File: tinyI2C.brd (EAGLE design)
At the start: 100 x 80 mm, 0 parts

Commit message: sch and brd update
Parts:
- added C1, C2, C3, C4, C6: 1005, rcl:C1005
- added C5: 1608, rcl:C1608
- added IC1: 74ABT125BQ, 74xx-eu_local:DHVQFN14
- added IC2: TPS76318, texas:SOT23-DBV
- added R1, R2: 220/1005, rcl:R1005
- added R10, R3, R4, R5, R6, R7, R8, R9: 10k/1005, rcl:R1005
- added TP1, TP2, TP3, TP8, TP9: TPTP07R, testpad:TP07R
- added U1: LPC824M201JHI33, mbed-HDK:HVQFN33
- added X1, X3: TSW-112-02-S-S, con-samtec.local:TSW-112-02-S-S
- added X2: TSW-106-02-S-S-RA, con-samtec.local:TSW-106-02-S-S-RA
- added X4: TSW-102-02-S-S, con-samtec.local:TSW-102-02-S-S
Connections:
- new net !ISP!: R3.1, U1.2, X1.3
- new net !RESET!: R4.1, U1.3, X4.1
- new net 1.8V: C1.1, C2.1, C4.1, C6.1, IC1.14, IC2.5, R1.2, R10.2, R2.2, R3.2, R4.2, R5.2, R6.2, R7.2, R8.2, R9.2, TP2.TP, U1.19, U1.21, X1.1
- new net 5V: C5.1, IC2.1, IC2.3, TP1.TP, X2.3
- new net CTS<-: IC1.6, X2.2
- new net GND: C1.2, C2.2, C3.2, C4.2, C5.2, C6.2, IC1.1, IC1.10, IC1.13, IC1.4, IC1.7, IC1.EXP, IC2.2, TP3.TP, U1.20, U1.EXP, X1.2, X2.1, X4.2
- new net GPIO00: U1.32, X3.1
- new net GPIO01: U1.31, X3.2
- new net GPIO02: U1.30, X3.3
- new net GPIO03: U1.29, X3.4
- new net GPIO04: U1.28, X3.5
- new net GPIO05: U1.27, X3.6
- new net GPIO06: U1.26, X3.7
- new net GPIO07: U1.25, X3.8
- new net GPIO10: R10.1, U1.15, X1.12
- new net GPIO11: R9.1, U1.14, X1.11
- new net GPIO12: R8.1, U1.13, X1.10
- new net GPIO13: R7.1, U1.12, X1.9
- new net GPIO14: R6.1, U1.11, X1.8
- new net GPIO15: R5.1, U1.10, X1.7
- new net GPIO16: U1.5, X1.4
- new net I2C_SCL: R2.1, U1.9, X1.6
- new net I2C_SDA: R1.1, U1.8, X1.5
- new net N$1: C3.1, IC2.4
- new net RTS->: IC1.9, X2.6
- new net RX<-: IC1.11, X2.5
- new net SPI_CS: U1.17, X3.12
- new net SPI_MISO: U1.22, X3.10
- new net SPI_MOSI: U1.23, X3.9
- new net SPI_SCK: U1.18, X3.11
- new net SWCLK: TP8.TP, U1.6
- new net SWDIO: TP9.TP, U1.7
- new net TGT_CTS: IC1.8, U1.16
- new net TGT_RTS: IC1.5, U1.1
- new net TGT_RX: IC1.3, U1.24
- new net TGT_TX: IC1.12, U1.4
- new net TX->: IC1.2, X2.4
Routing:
- net 1.8V: track 0.00 -> 49.3 mm, vias 0 -> 15
- net TGT_CTS: track 0.00 -> 24.3 mm, vias 0 -> 2
- net SPI_CS: track 0.00 -> 19.7 mm
- net GPIO00: track 0.00 -> 18.6 mm, vias 0 -> 1
- net SPI_SCK: track 0.00 -> 17.9 mm
- net !RESET!: track 0.00 -> 17.8 mm, vias 0 -> 2
- net TGT_RX: track 0.00 -> 17.3 mm, vias 0 -> 2
- net GPIO01: track 0.00 -> 16.7 mm, vias 0 -> 1
- net !ISP!: track 0.00 -> 15.6 mm, vias 0 -> 2
- net GND: track 0.00 -> 15.6 mm, vias 0 -> 13
- net TGT_TX: track 0.00 -> 15.5 mm, vias 0 -> 2
- net CTS<-: track 0.00 -> 15.1 mm
- net GPIO02: track 0.00 -> 15.0 mm
- net GPIO10: track 0.00 -> 14.6 mm
- net GPIO11: track 0.00 -> 14.1 mm
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- added copper zone on layer 16, net 1.8V
- added copper zone on layer 1, net GND
- added copper zone on layer 16, net GND
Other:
- board size 100 x 80 mm -> 80.8 x 80 mm

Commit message: fiducials
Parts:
- added TP4, TP5: TPTP10R, testpad:TP10R
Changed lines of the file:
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@@
 <hole x="5" y="75" drill="4"/>
 <hole x="75.8" y="5" drill="4"/>
-<polygon width="0.2" layer="29">
+<polygon width="0" layer="29">
 <vertex x="69.8" y="4"/>
 <vertex x="69.8" y="6"/>
@@
 <vertex x="71.8" y="4"/>
 </polygon>
-<polygon width="0.2" layer="29">
+<polygon width="0" layer="29">
 <vertex x="14" y="74"/>
 <vertex x="14" y="76"/>
@@
 <attribute name="VALUE" x="17.72" y="20.355" size="1.27" layer="27" rot="R180"/>
 </element>
+<element name="TP4" library="testpad" package="TP10R" value="TPTP10R" x="15" y="75" smashed="yes">
+<attribute name="TP_SIGNAL_NAME" value="" x="15" y="73.095" size="1" layer="37"/>
+<attribute name="VALUE" x="14.746" y="74.492" size="0.0254" layer="27"/>
+</element>
+<element name="TP5" library="testpad" package="TP10R" value="TPTP10R" x="70.8" y="5" smashed="yes">
+<attribute name="TP_SIGNAL_NAME" value="" x="70.8" y="3.095" size="1" layer="37"/>
+<attribute name="VALUE" x="70.546" y="4.492" size="0.0254" layer="27"/>
+</element>
 </elements>

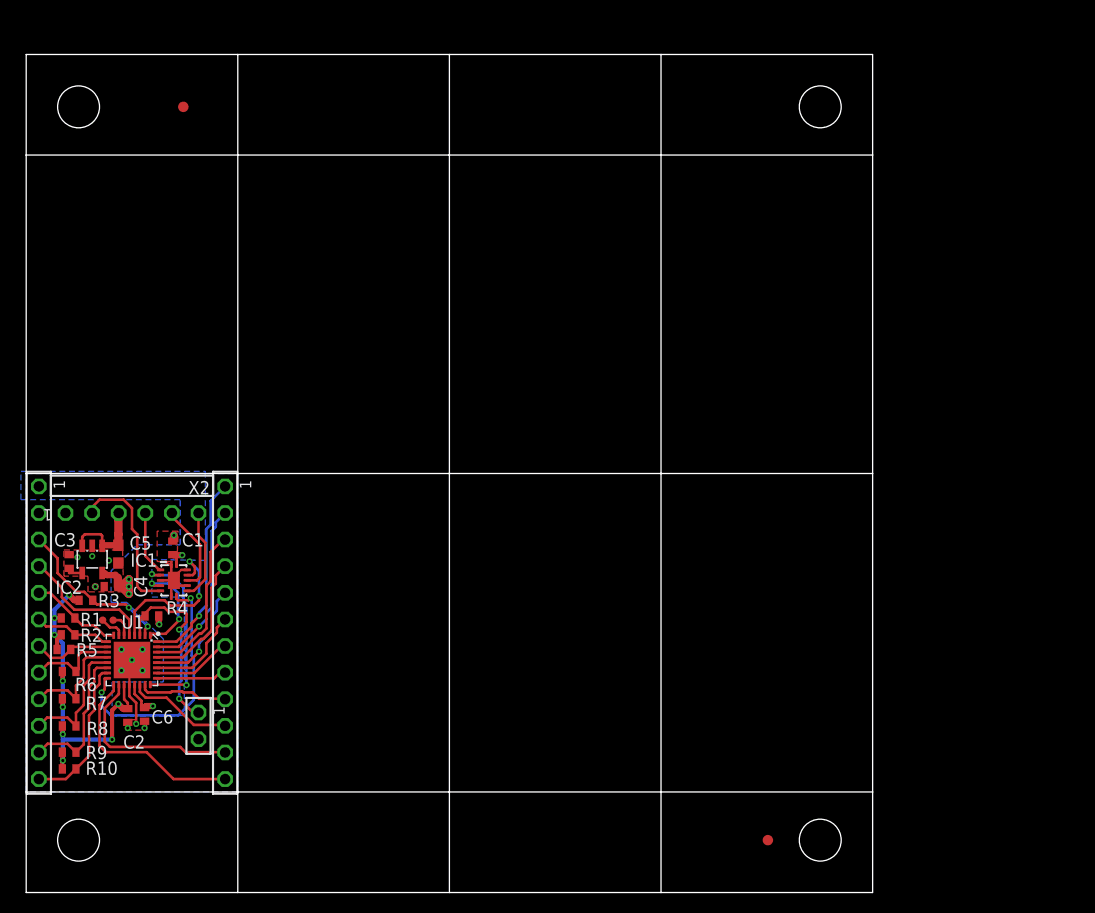
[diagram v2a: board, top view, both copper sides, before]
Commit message: panelize update
each edge has 0.4mm margin
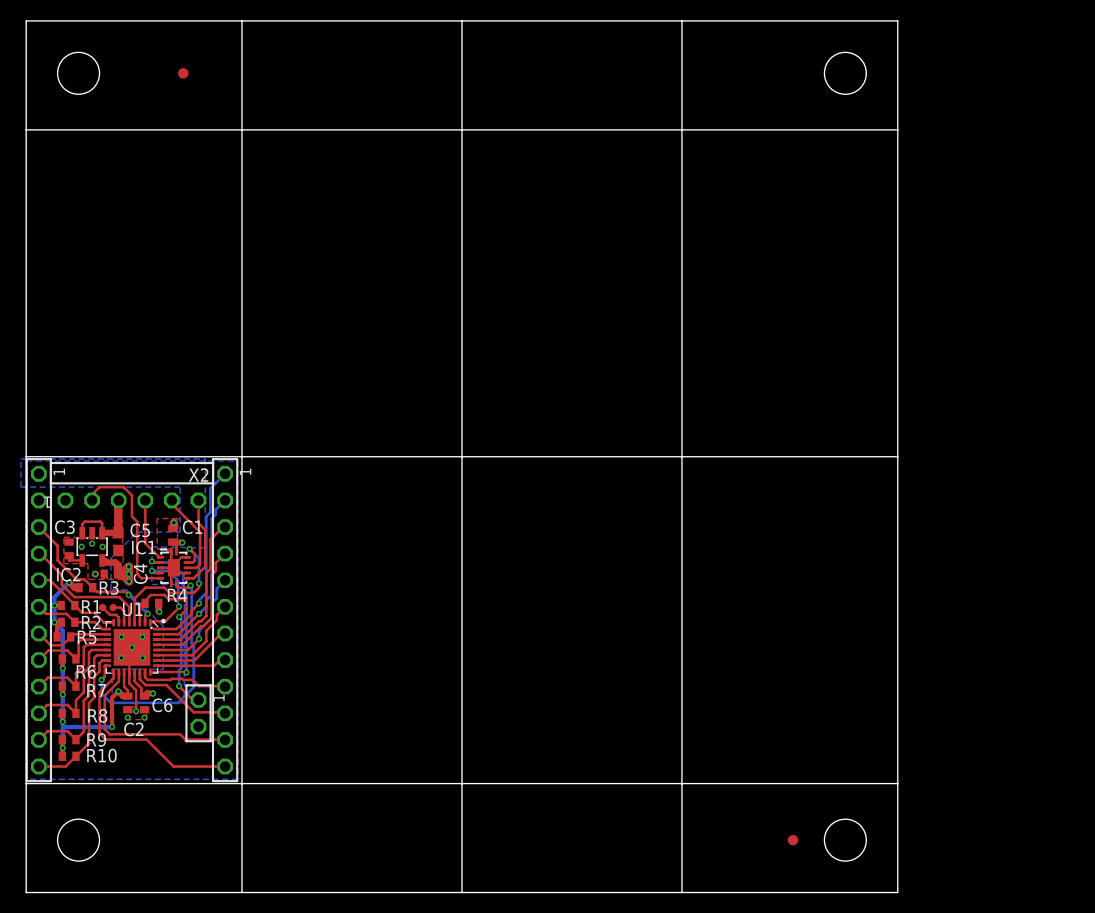
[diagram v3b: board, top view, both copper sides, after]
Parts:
- moved TP4 3.20 mm to (15.0, 78.2)
- moved TP5 2.40 mm to (73.2, 5.00)
- moved C1 1.20 mm to (14.0, 34.1)
- moved C2 1.20 mm to (9.70, 18.1)
- moved C5 1.20 mm to (8.80, 33.5)
- moved R3 1.20 mm to (5.70, 29.1)
- moved R4 1.20 mm to (12.0, 27.6)
- moved X2 1.20 mm to (10.1, 39.0)
- moved R8 1.20 mm to (4.10, 17.1)
- moved C4 1.20 mm to (8.10, 30.4)
- moved IC1 1.20 mm to (14.1, 31.0)
- moved IC2 1.20 mm to (6.30, 33.0)
- moved R1 1.20 mm to (4.00, 27.4)
- moved R10 1.20 mm to (4.10, 13.0)
- moved R2 1.20 mm to (4.00, 25.8)
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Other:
- board size 80.8 x 80 mm -> 83.2 x 83.2 mm

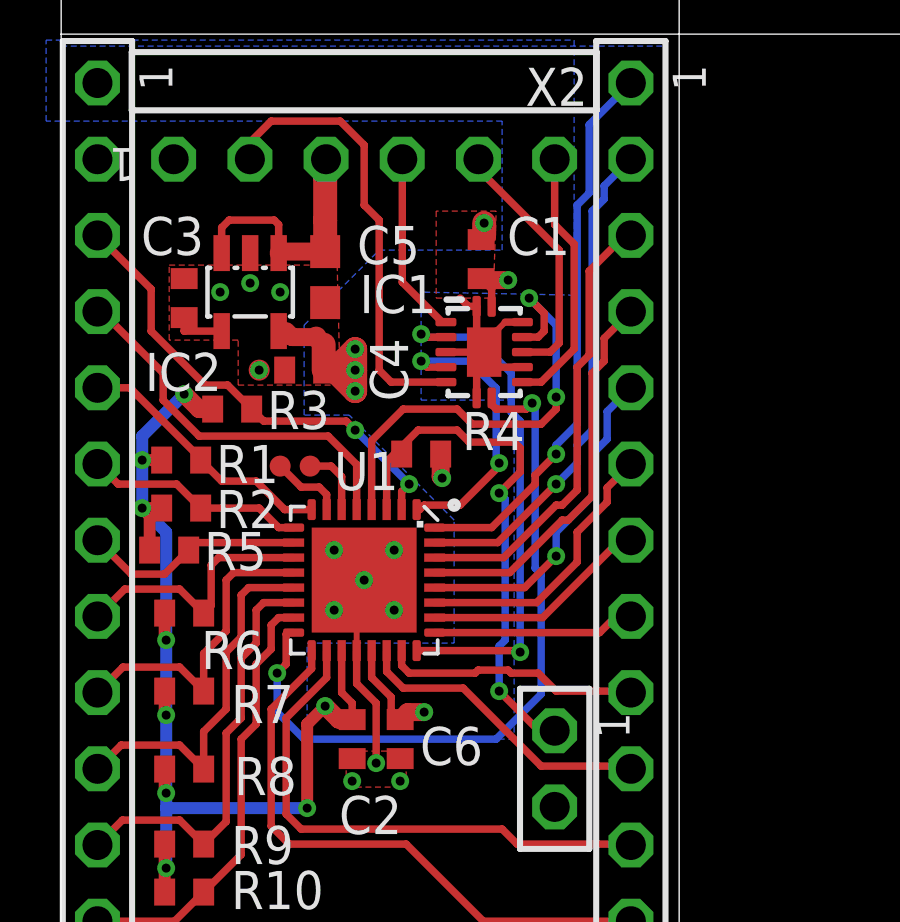
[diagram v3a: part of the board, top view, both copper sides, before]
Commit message: 1.8V trace get wider
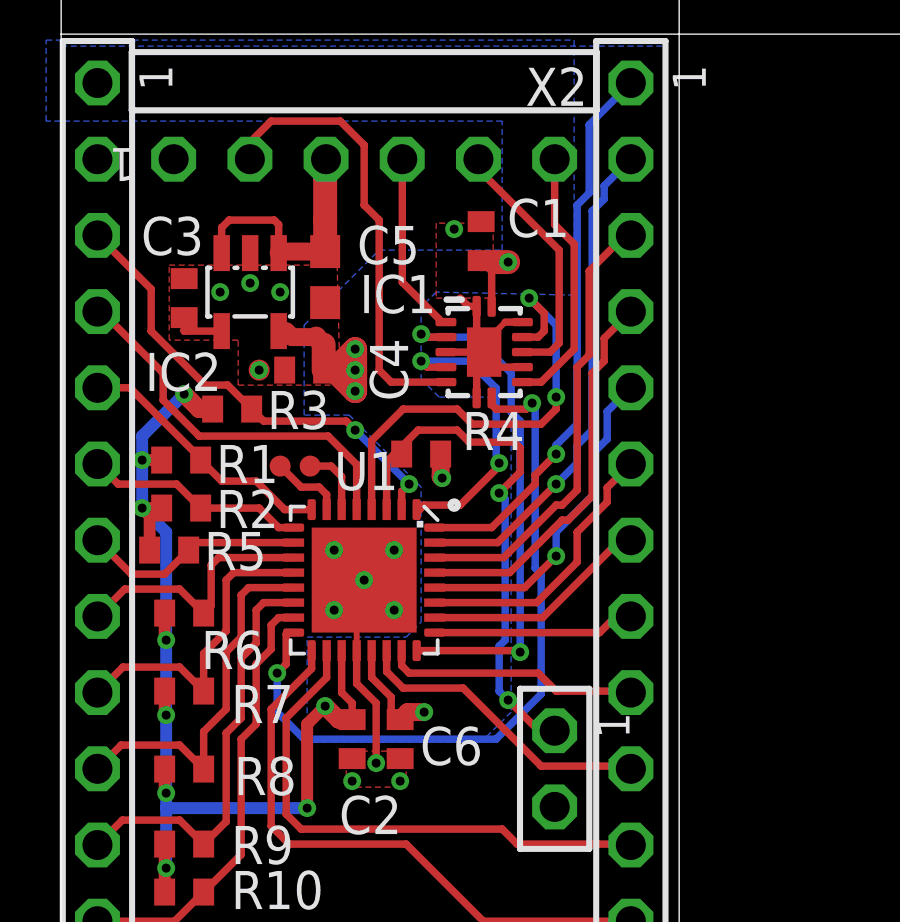
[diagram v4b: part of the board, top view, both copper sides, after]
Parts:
- moved C1 0.60 mm to (14.0, 34.7)
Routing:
- net 1.8V: track 49.4 -> 50.1 mm
- net GND: track 15.6 -> 15.0 mm
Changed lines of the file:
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@@
 <attribute name="VALUE" x="8.205" y="36.429" size="1.27" layer="27" rot="R180"/>
 </element>
-<element name="C1" library="rcl" package="C1005" value="1005" x="14" y="34.1" smashed="yes" rot="R90">
-<attribute name="NAME" x="14.865" y="34.235" size="1.27" layer="25" font="vector" ratio="10"/>
-<attribute name="VALUE" x="15.905" y="33.465" size="1.27" layer="27" rot="R90"/>
+<element name="C1" library="rcl" package="C1005" value="1005" x="14" y="34.7" smashed="yes" rot="R90">
+<attribute name="NAME" x="14.865" y="34.835" size="1.27" layer="25" font="vector" ratio="10"/>
+<attribute name="VALUE" x="15.905" y="34.065" size="1.27" layer="27" rot="R90"/>
 </element>
 <element name="C2" library="rcl" package="C1005" value="1005" x="9.7" y="18.1" smashed="yes" rot="R270">
@@
 <contactref element="C2" pad="2"/>
 <contactref element="TP3" pad="TP"/>
-<via x="14.1" y="35.3" extent="1-16" drill="0.3"/>
+<via x="13.1" y="35.1" extent="1-16" drill="0.3"/>
 <via x="11.1" y="22.4" extent="1-16" drill="0.3"/>
 <via x="11.1" y="24.4" extent="1-16" drill="0.3"/>
@@
 <contactref element="C3" pad="2"/>
 <via x="5.3" y="33" extent="1-16" drill="0.3"/>
-<wire x1="14" y1="34.75" x2="14.1" y2="34.9" width="0.6" layer="1"/>
-<wire x1="14.1" y1="34.9" x2="14.1" y2="35.3" width="0.8" layer="1"/>
 <contactref element="X1" pad="2"/>
 <contactref element="C6" pad="2"/>
@@
 <vertex x="12.5" y="32.8"/>
 <vertex x="14.4" y="32.8"/>
-<vertex x="14.5" y="35.7"/>
-<vertex x="12.5" y="35.7"/>
+<vertex x="14.4" y="35.3"/>
+<vertex x="12.5" y="35.3"/>
 </polygon>
 <contactref element="IC1" pad="7"/>
@@
 <contactref element="C2" pad="1"/>
 <contactref element="TP2" pad="TP"/>
-<via x="14.9" y="33.4" extent="1-16" drill="0.3"/>
+<via x="14.9" y="34" extent="1-16" drill="0.3"/>
 <contactref element="R1" pad="2"/>
 <contactref element="R2" pad="2"/>
@@
 <vertex x="17.1" y="41.4"/>
 <vertex x="17.1" y="32.9"/>
-<vertex x="12" y="33"/>
-<vertex x="12" y="29.4"/>
-<vertex x="15.1" y="29.4"/>
-<vertex x="15.1" y="18.1"/>
-<vertex x="8.2" y="18.1"/>
-<vertex x="8.2" y="21.3"/>
-<vertex x="13.1" y="21.3"/>
-<vertex x="13.1" y="25.4"/>
+<vertex x="12.5" y="33"/>
+<vertex x="12" y="32.5"/>
+<vertex x="12" y="30.1"/>
+<vertex x="12.6" y="29.5"/>
+<vertex x="15" y="29.5"/>
+<vertex x="15" y="19"/>
+<vertex x="14" y="18"/>
+<vertex x="8.2" y="18"/>
+<vertex x="8.2" y="21.5"/>
+<vertex x="11.5" y="21.5"/>
+<vertex x="12" y="22"/>
+<vertex x="12" y="26.5"/>
 <vertex x="9.6" y="28.9"/>
 <vertex x="8.1" y="28.9"/>
@@
 <wire x1="7.5" y1="31.7" x2="7.7" y2="31.5" width="0.6" layer="1"/>
 <wire x1="7.7" y1="31.5" x2="8.5" y2="31.5" width="0.6" layer="1"/>
-<wire x1="14.35" y1="33.1" x2="14" y2="33.45" width="0.25" layer="1"/>
 <wire x1="12.65" y1="27.6" x2="12.65" y2="26.85" width="0.6" layer="1"/>
 <wire x1="12.65" y1="26.85" x2="12.7" y2="26.8" width="0.6" layer="1"/>
@@
 <wire x1="2.7" y1="28.2" x2="4.1" y2="29.6" width="0.4" layer="16"/>
 <wire x1="3.35" y1="27.4" x2="2.7" y2="27.4" width="0.4" layer="1"/>
-<wire x1="14.9" y1="33.4" x2="14.05" y2="33.4" width="0.6" layer="1"/>
-<wire x1="14.05" y1="33.4" x2="14" y2="33.45" width="0.6" layer="1"/>
 <via x="8.2" y="15.8" extent="1-16" drill="0.3" diameter="0.6"/>
 <wire x1="8.2" y1="15.8" x2="3.5" y2="15.8" width="0.4" layer="16"/>
@@
 <contactref element="X1" pad="1"/>
 <contactref element="IC1" pad="14"/>
-<wire x1="14.35" y1="32.525" x2="14.35" y2="33.1" width="0.25" layer="1"/>
+<wire x1="14.35" y1="32.525" x2="14.35" y2="33.7" width="0.25" layer="1"/>
+<wire x1="14.9" y1="34" x2="14.5" y2="34" width="0.8" layer="1"/>
+<wire x1="14.5" y1="34" x2="14" y2="34" width="0.6" layer="1"/>
+<wire x1="14" y1="34" x2="14" y2="34.05" width="0.6" layer="1"/>
+<wire x1="14.35" y1="33.7" x2="14" y2="34.05" width="0.25" layer="1"/>
 </signal>
 <signal name="TGT_TX">
@@
 <wire x1="14.8" y1="21.4" x2="14.6" y2="21.2" width="0.25" layer="16"/>
 <wire x1="14.6" y1="21.2" x2="14.6" y2="19.7" width="0.25" layer="16"/>
+<wire x1="14.6" y1="19.7" x2="14.9" y2="19.4" width="0.25" layer="16"/>
 <wire x1="11.1" y1="27.6" x2="11.35" y2="27.6" width="0.25" layer="1"/>
-<via x="14.6" y="19.7" extent="1-16" drill="0.3"/>
-<wire x1="14.6" y1="19.7" x2="15.92" y2="18.38" width="0.25" layer="1"/>
+<via x="14.9" y="19.4" extent="1-16" drill="0.3"/>
+<wire x1="14.9" y1="19.4" x2="15.92" y2="18.38" width="0.25" layer="1"/>
 <contactref element="X4" pad="1"/>
 <wire x1="15.92" y1="18.38" x2="16.45" y2="18.38" width="0.25" layer="1"/>
@@
 <contactref element="X3" pad="9"/>
 <wire x1="11.35" y1="20.55" x2="11.6" y2="20.3" width="0.25" layer="1"/>
-<wire x1="11.6" y1="20.3" x2="13.8" y2="20.3" width="0.25" layer="1"/>
-<wire x1="13.8" y1="20.3" x2="13.9" y2="20.4" width="0.25" layer="1"/>
-<wire x1="13.9" y1="20.4" x2="14.9" y2="20.4" width="0.25" layer="1"/>
-<wire x1="14.9" y1="20.4" x2="15" y2="20.3" width="0.25" layer="1"/>
-<wire x1="15" y1="20.3" x2="15.9" y2="20.3" width="0.25" layer="1"/>
+<wire x1="11.6" y1="20.3" x2="15.9" y2="20.3" width="0.25" layer="1"/>
 <wire x1="15.9" y1="20.3" x2="16.5" y2="19.7" width="0.25" layer="1"/>
 <wire x1="16.5" y1="19.7" x2="18.94" y2="19.7" width="0.25" layer="1"/>
